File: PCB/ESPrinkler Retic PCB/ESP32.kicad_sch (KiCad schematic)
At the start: 2 parts, among them J4 Conn_01x19, J5 Conn_01x19

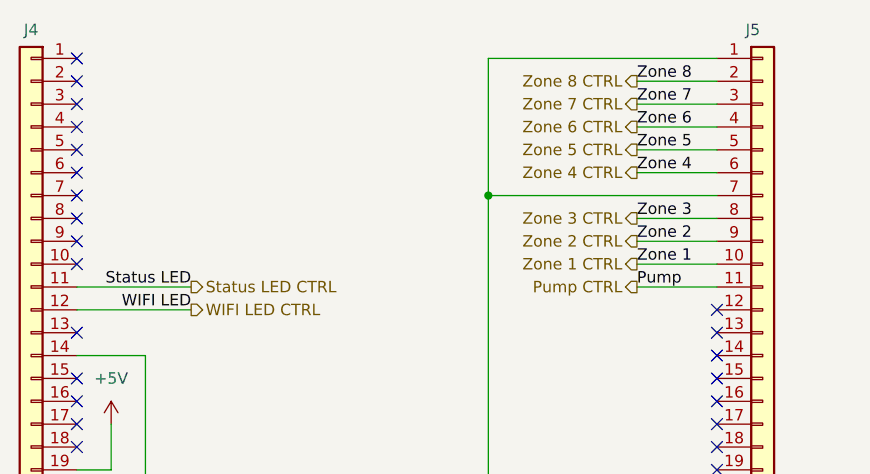
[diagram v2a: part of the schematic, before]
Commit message: Labelling as V2.0
Repo needs to change, I have been using it poorly. V2.0 will be the next "main branch". After that, forks will be used instead

Also in this commit, I have updated the custom footprints and updated the links to them in the project.
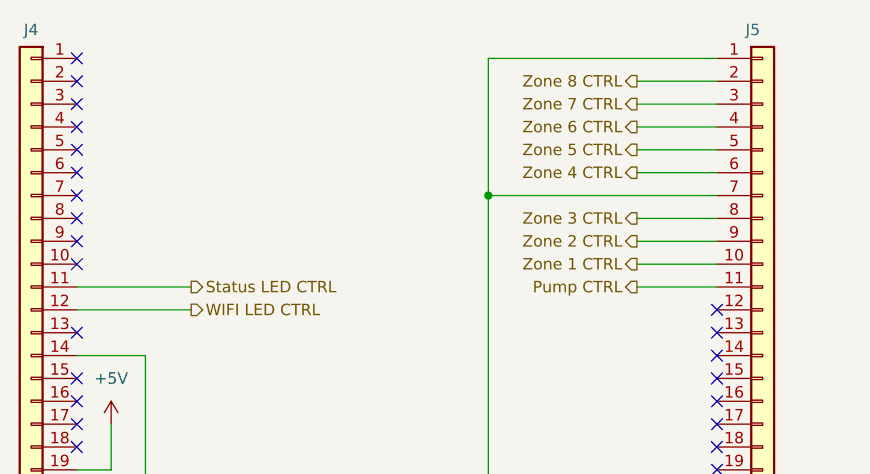
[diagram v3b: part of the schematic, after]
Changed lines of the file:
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@@
 		(title "ESPrinkler Retic Controller")
 		(date "2025-06-01")
-		(rev "1.1")
+		(rev "2.0")
+		(comment 1 "Designed by: Slippery-Carrot")
+		(comment 3 "github.com/slippery-carrot/ESPrinkler-Retic-Controller")
 	)
 	(text "GPIO6-11 & GPIO34-39 cannot be used"
@@
 		)
 	)
-	(label "Pump"
-		(at 171.45 87.63 0)
-		(effects
-			(font
-				(size 1.27 1.27)
-			)
-			(justify left bottom)
-		)
-	)
-	(label "Zone 1"
-		(at 171.45 85.09 0)
-		(effects
-			(font
-				(size 1.27 1.27)
-			)
-			(justify left bottom)
-		)
-	)
-	(label "Zone 6"
-		(at 171.45 69.85 0)
-		(effects
-			(font
-				(size 1.27 1.27)
-			)
-			(justify left bottom)
-		)
-	)
-	(label "WIFI LED"
-		(at 121.92 90.17 180)
-		(effects
-			(font
-				(size 1.27 1.27)
-			)
-			(justify right bottom)
-		)
-	)
-	(label "Zone 2"
-		(at 171.45 82.55 0)
-		(effects
-			(font
-				(size 1.27 1.27)
-			)
-			(justify left bottom)
-		)
-	)
-	(label "Zone 4"
-		(at 171.45 74.93 0)
-		(effects
-			(font
-				(size 1.27 1.27)
-			)
-			(justify left bottom)
-		)
-	)
-	(label "Zone 5"
-		(at 171.45 72.39 0)
-		(effects
-			(font
-				(size 1.27 1.27)
-			)
-			(justify left bottom)
-		)
-	)
-	(label "Zone 7"
-		(at 171.45 67.31 0)
-		(effects
-			(font
-				(size 1.27 1.27)
-			)
-			(justify left bottom)
-		)
-	)
-	(label "Zone 3"
-		(at 171.45 80.01 0)
-		(effects
-			(font
-				(size 1.27 1.27)
-			)
-			(justify left bottom)
-		)
-	)
-	(label "Zone 8"
-		(at 171.45 64.77 0)
-		(effects
-			(font
-				(size 1.27 1.27)
-			)
-			(justify left bottom)
-		)
-	)
-	(label "Status LED"
-		(at 121.92 87.63 180)
-		(effects
-			(font
-				(size 1.27 1.27)
-			)
-			(justify right bottom)
-		)
-	)

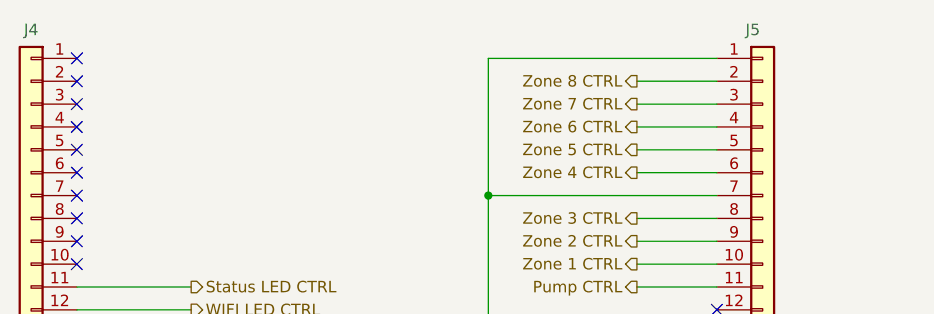
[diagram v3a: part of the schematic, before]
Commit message: Change 12-pin connector
Change from screw terminal barrier block to a wire-to-board screw terminal block.

Opted for a 3-pin terminal block, 4 of them due the 12-pin not being available through lcsc, to get a total of 12 when connected together. Makes the design a bit confusing but the BOM is accurate
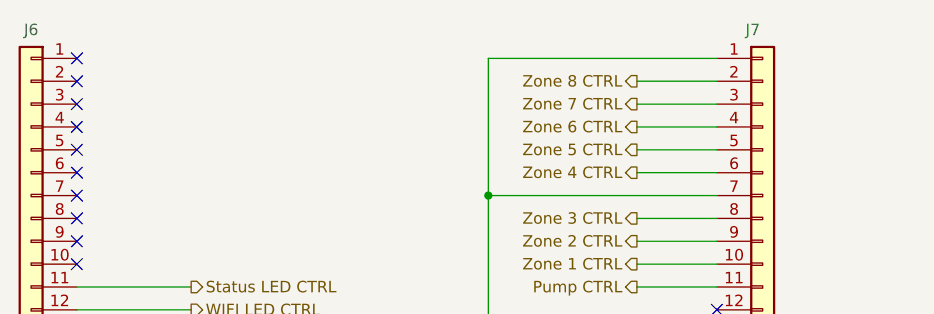
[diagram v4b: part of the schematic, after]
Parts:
- renumbered J4 to J6, J5 to J7
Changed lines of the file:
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@@
 		(in_pos_files yes)
 		(dnp no)
-		(property "Reference" "J5"
+		(property "Reference" "J7"
 			(at 183.515 59.055 0)
 			(show_name no)
@@
 			(project "ESPrinkler Retic PCB"
 				(path "/3c6b8bc3-d793-478e-a69e-22171e9bcb1b/d67bcfb8-08ed-4cad-86f9-861082825312"
-					(reference "J5")
+					(reference "J7")
 					(unit 1)
 				)
@@
 		(in_pos_files yes)
 		(dnp no)
-		(property "Reference" "J4"
+		(property "Reference" "J6"
 			(at 104.14 59.055 0)
 			(show_name no)
@@
 			(project "ESPrinkler Retic PCB"
 				(path "/3c6b8bc3-d793-478e-a69e-22171e9bcb1b/d67bcfb8-08ed-4cad-86f9-861082825312"
-					(reference "J4")
+					(reference "J6")
 					(unit 1)
 				)

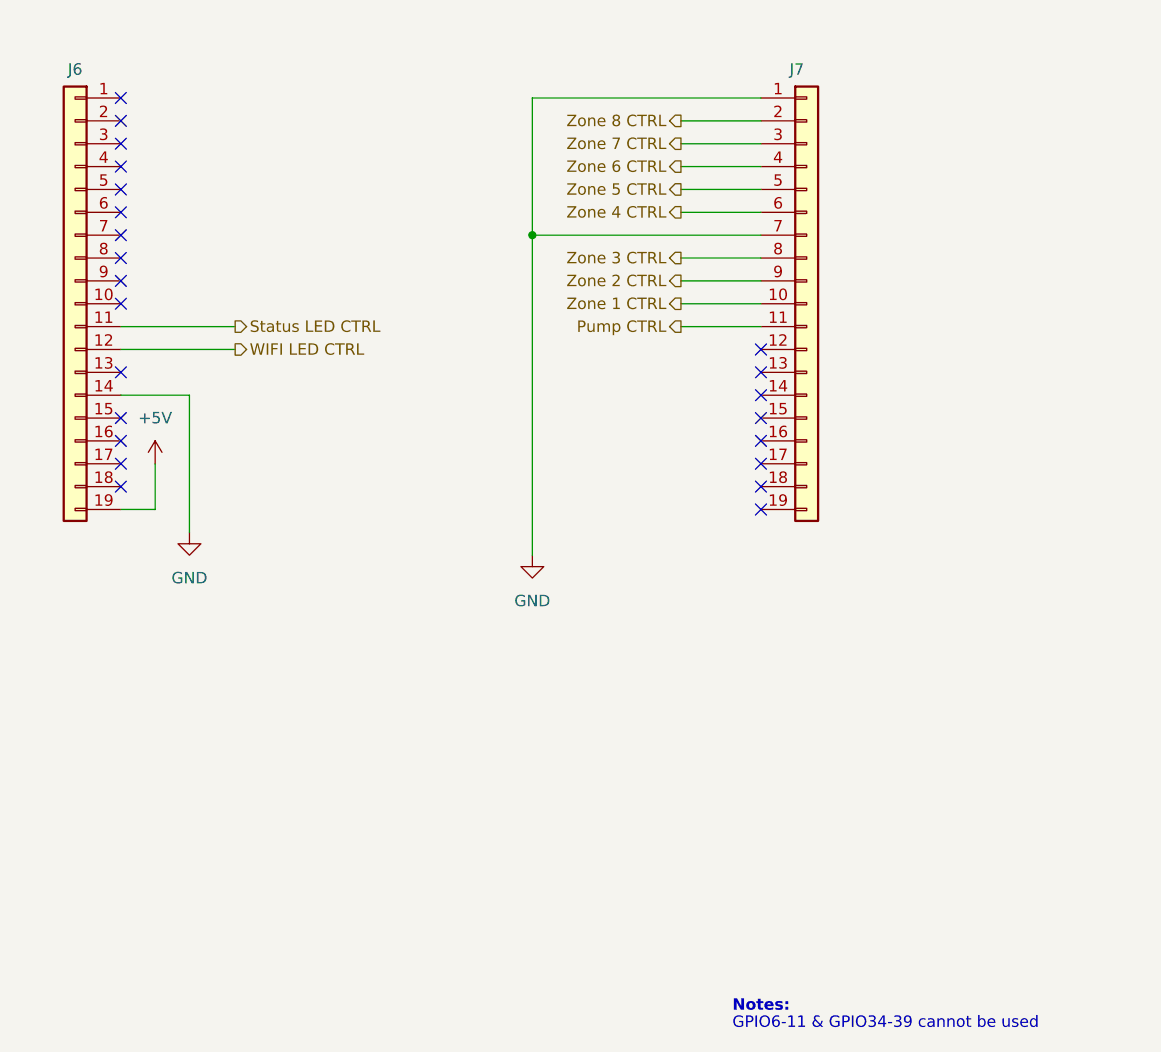
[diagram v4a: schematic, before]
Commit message: Change mounting holes
Change mounting holes to M3.2 with exposed pads and vias. Add them to schematic for reference
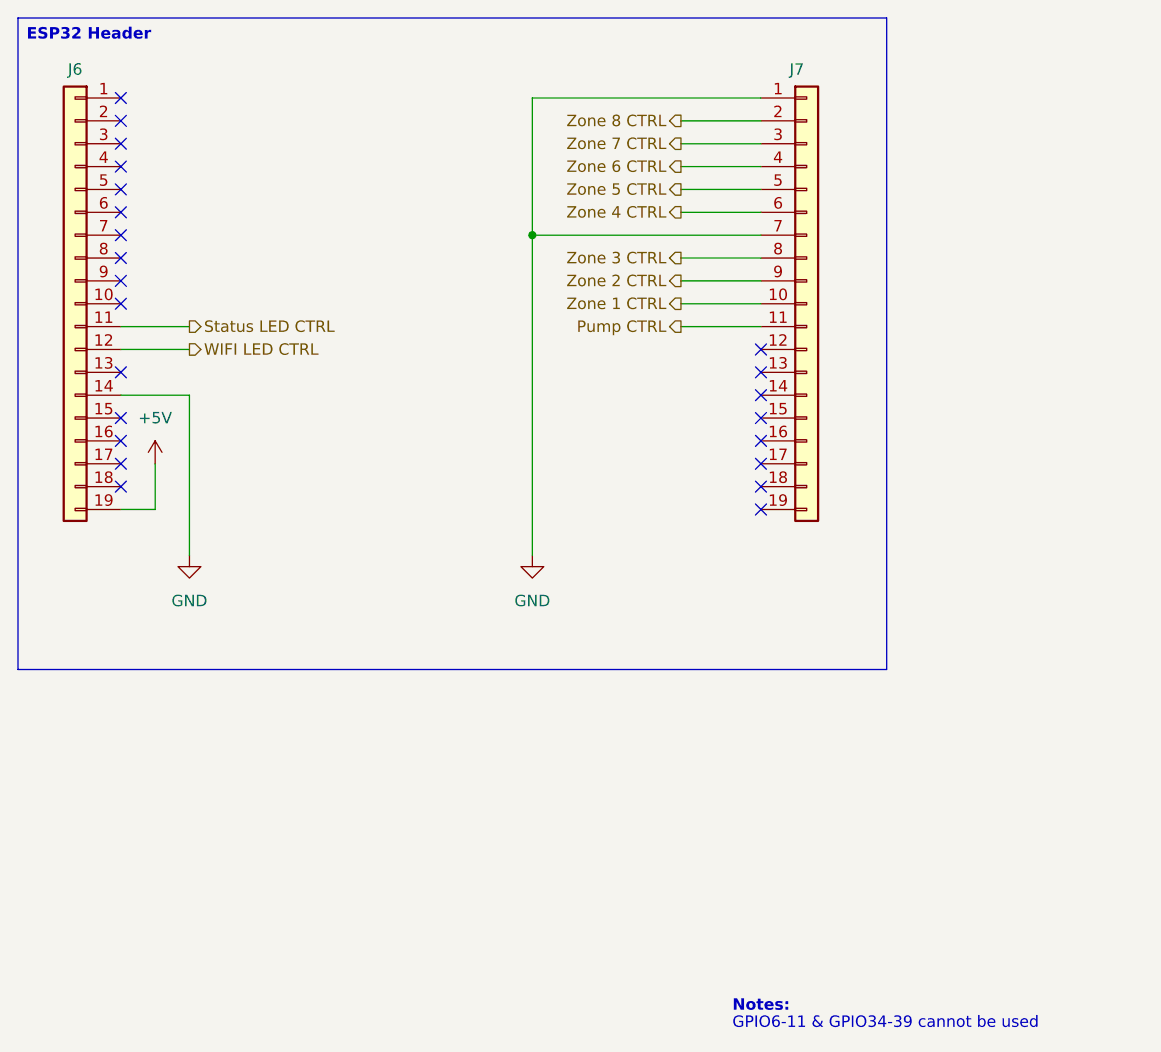
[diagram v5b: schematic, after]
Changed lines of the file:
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@@
+		)
+	)
+	(text_box "ESP32 Header"
+		(exclude_from_sim no)
+		(at 97.79 53.34 0)
+		(size 96.52 72.39)
+		(margins 0.9525 0.9525 0.9525 0.9525)
+		(stroke
+			(width 0)
+			(type solid)
+		)
+		(fill
+			(type none)
+		)
+		(effects
+			(font
+				(size 1.27 1.27)
+				(thickness 0.254)
+				(bold yes)
+			)
+			(justify left top)
 		)
 	)
@@
 	(wire
 		(pts
-			(xy 109.22 87.63) (xy 121.92 87.63)
+			(xy 109.22 87.63) (xy 116.84 87.63)
 		)
 		(stroke
@@
 	(wire
 		(pts
-			(xy 109.22 90.17) (xy 121.92 90.17)
+			(xy 109.22 90.17) (xy 116.84 90.17)
 		)
 		(stroke
@@
 	(wire
 		(pts
-			(xy 116.84 95.25) (xy 116.84 110.49)
+			(xy 116.84 95.25) (xy 116.84 113.03)
 		)
 		(stroke
@@
 	(hierarchical_label "Status LED CTRL"
 		(shape output)
-		(at 121.92 87.63 0)
+		(at 116.84 87.63 0)
 		(effects
 			(font
@@
 	(hierarchical_label "WIFI LED CTRL"
 		(shape output)
-		(at 121.92 90.17 0)
+		(at 116.84 90.17 0)
 		(effects
 			(font
@@
 	(symbol
 		(lib_id "power:GND")
-		(at 116.84 110.49 0)
+		(at 116.84 113.03 0)
 		(unit 1)
 		(body_style 1)
@@
 		(fields_autoplaced yes)
 		(property "Reference" "#PWR048"
-			(at 116.84 116.84 0)
+			(at 116.84 119.38 0)
 			(hide yes)
 			(show_name no)
@@
 		)
 		(property "Value" "GND"
-			(at 116.84 115.57 0)
+			(at 116.84 118.11 0)
 			(show_name no)
 			(do_not_autoplace no)
@@
 		)
 		(property "Footprint" ""
-			(at 116.84 110.49 0)
+			(at 116.84 113.03 0)
 			(hide yes)
 			(show_name no)
@@
 		)
 		(property "Datasheet" ""
-			(at 116.84 110.49 0)
+			(at 116.84 113.03 0)
 			(hide yes)
 			(show_name no)
@@
 		)
 		(property "Description" "Power symbol creates a global label with name \"GND\" , ground"
-			(at 116.84 110.49 0)
-			(hide yes)
-			(show_name no)
+			(at 116.84 113.03 0)
+			(hide yes)
+			(show_name no)
